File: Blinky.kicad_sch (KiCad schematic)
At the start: 0 parts

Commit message: Created schematic and added vicor and precharge stuff, still need to add board connectors for pacmania
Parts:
- added C1, C2: 1uF, Capacitor_THT:C_Rect_L18.0mm_W8.0mm_P15.00mm_FKS3_FKP3, symbol Device:C_Small
- added C4: 4700uF, Capacitor_THT:C_Radial_D12.5mm_H25.0mm_P5.00mm, symbol Device:C_Small
- added C5: 100uF, Capacitor_THT:C_Radial_D12.5mm_H25.0mm_P5.00mm, symbol Device:C_Small
- added D3: LTST-C171KRKT, LED_SMD:LED_0805_2012Metric, symbol Device:LED
- added D4, D5: BZT52C5V1, Diode_SMD:D_SOD-123, symbol Device:D_Zener
- added J1: DTF13-4P-G003, AERO_Connectors:DTF13-4P-G003, symbol AERO_Connectors:DTF13-4P-G003
- added L1: 1uH, Inductor_SMD:L_1008_2520Metric_Pad1.43x2.20mm_HandSolder, symbol Device:L_Small
- added L2: SLC7649S-151KLC, AERO_Inductors:SLC7649S-151KLC, symbol AERO_Inductors:SLC7649S-151KLC
- added Q1, Q2: IPD90P03P404ATMA2, AERO_Transistors:IPD90P03P404ATMA2, symbol AERO_Transistors:IPD90P03P404ATMA2
- added R1, R2: MP925-5.00K-1%, AERO_Resistors:MP925-5.00K-1%_TabUp, symbol AERO_Resistors:MP925-5.00K-1%
- added R11, R3: 1, Resistor_SMD:R_2512_6332Metric_Pad1.40x3.35mm_HandSolder, symbol Device:R_US
- added R12: 500, Resistor_SMD:R_0805_2012Metric_Pad1.20x1.40mm_HandSolder, symbol Device:R_US
- added R13, R14: 22k, Resistor_SMD:R_0603_1608Metric_Pad0.98x0.95mm_HandSolder, symbol Device:R_US
- added U1: DCM4623TD2J13D0T70, AERO_Regulators:DCM4623TD2J13D0T70, symbol AERO_Regulators:DCM4623TD2J13D0T70
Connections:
- new net: D3.1 (K), R12.1
- new net: D4.2 (A), Q1.2 (G), R13.1
- new net: C1.1, C2.1, L1.2, R3.1, U1.1 (+IN)
- new net: D5.2 (A), Q2.2 (G), R14.1
- new net EN_HV: U1.3 (EN)
- new net FAULT_HV: U1.4 (FT)
- new net INVERTER+: L1.1, R1.2, R3.2
- new net INVERTER-: C1.2, C2.2, R2.1, U1.5 (-IN)
- new net LV_GND: C4.2, C5.2, R12.2, R13.2, R14.2, U1.9 (-OUT)
- new net PRECHARGE_RELAY: R1.1, R2.2
- new net TRIM_HV: U1.2 (TR)
- new net VICOR_FILTERED: C5.1, D3.2 (A), L2.2, Q1.1 (D), Q2.1 (D), R11.1
- new net VICOR_OUT: D4.1 (K), D5.1 (K), J1.1 (Pin_1), J1.2 (Pin_2), J1.3 (Pin_3), J1.4 (Pin_4), Q1.3 (S), Q2.3 (S)
- new net VICOR_RAW: C4.1, L2.1, R11.2, U1.8 (+OUT)
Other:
- note added: "0.25W"
- note added: "500V-rated caps"
- note added: "HIGH VOLTAGE"
- note added: "HV->12V DC-DC"
- note added: "Input Filtering"
- note added: "Output Filtering"
- note added: "max input current ~= 0.81 A"

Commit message: Added connectors
This light will be the death of me
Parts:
- added J2, J3, J4: Conn_01x01, symbol Connector_Generic:Conn_01x01
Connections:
- net INVERTER+: now also J2.1 (Pin_1)
- net INVERTER-: now also J3.1 (Pin_1)
- net PRECHARGE_RELAY: now also J4.1 (Pin_1)

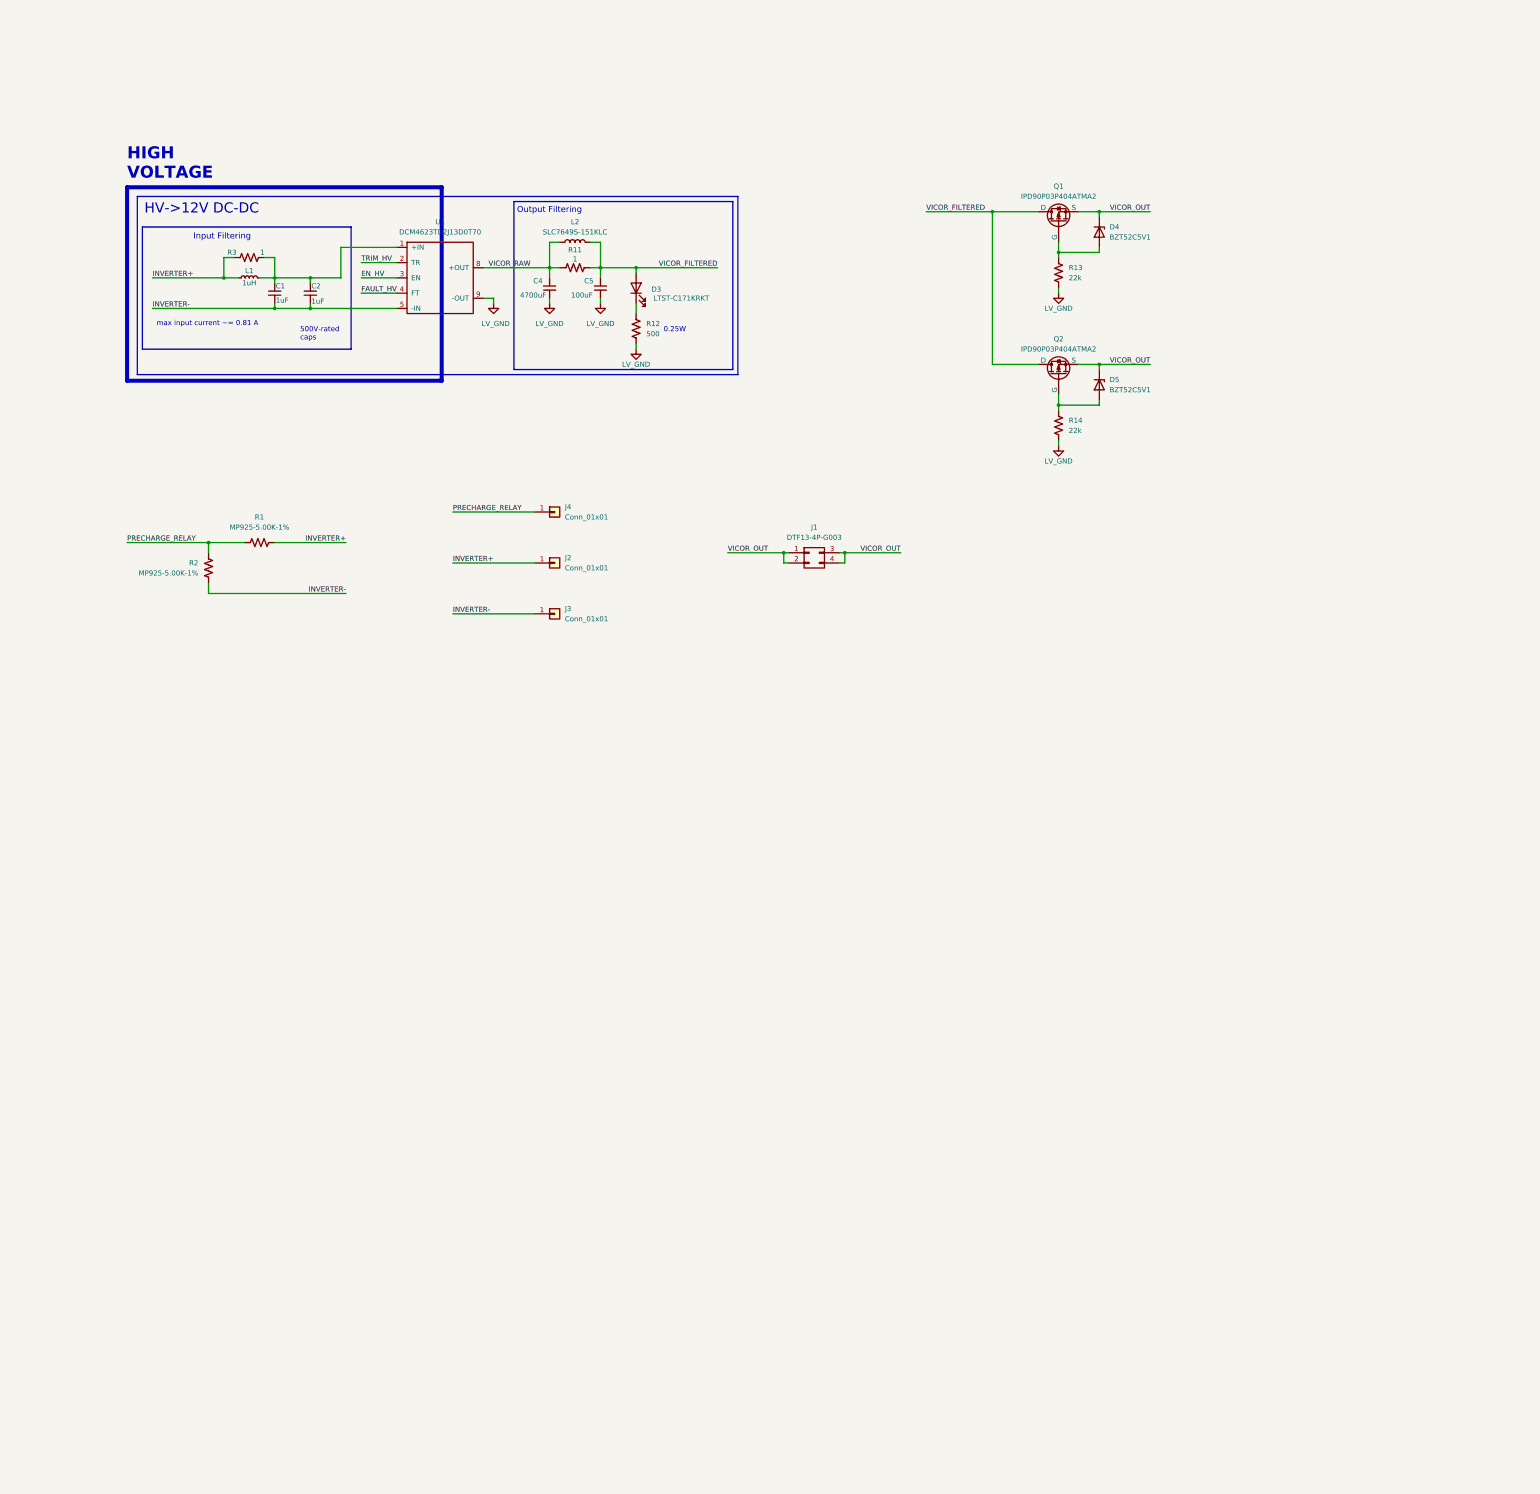
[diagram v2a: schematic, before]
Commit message: Added more final circuit for HV indicator LED, need to update values and footprints
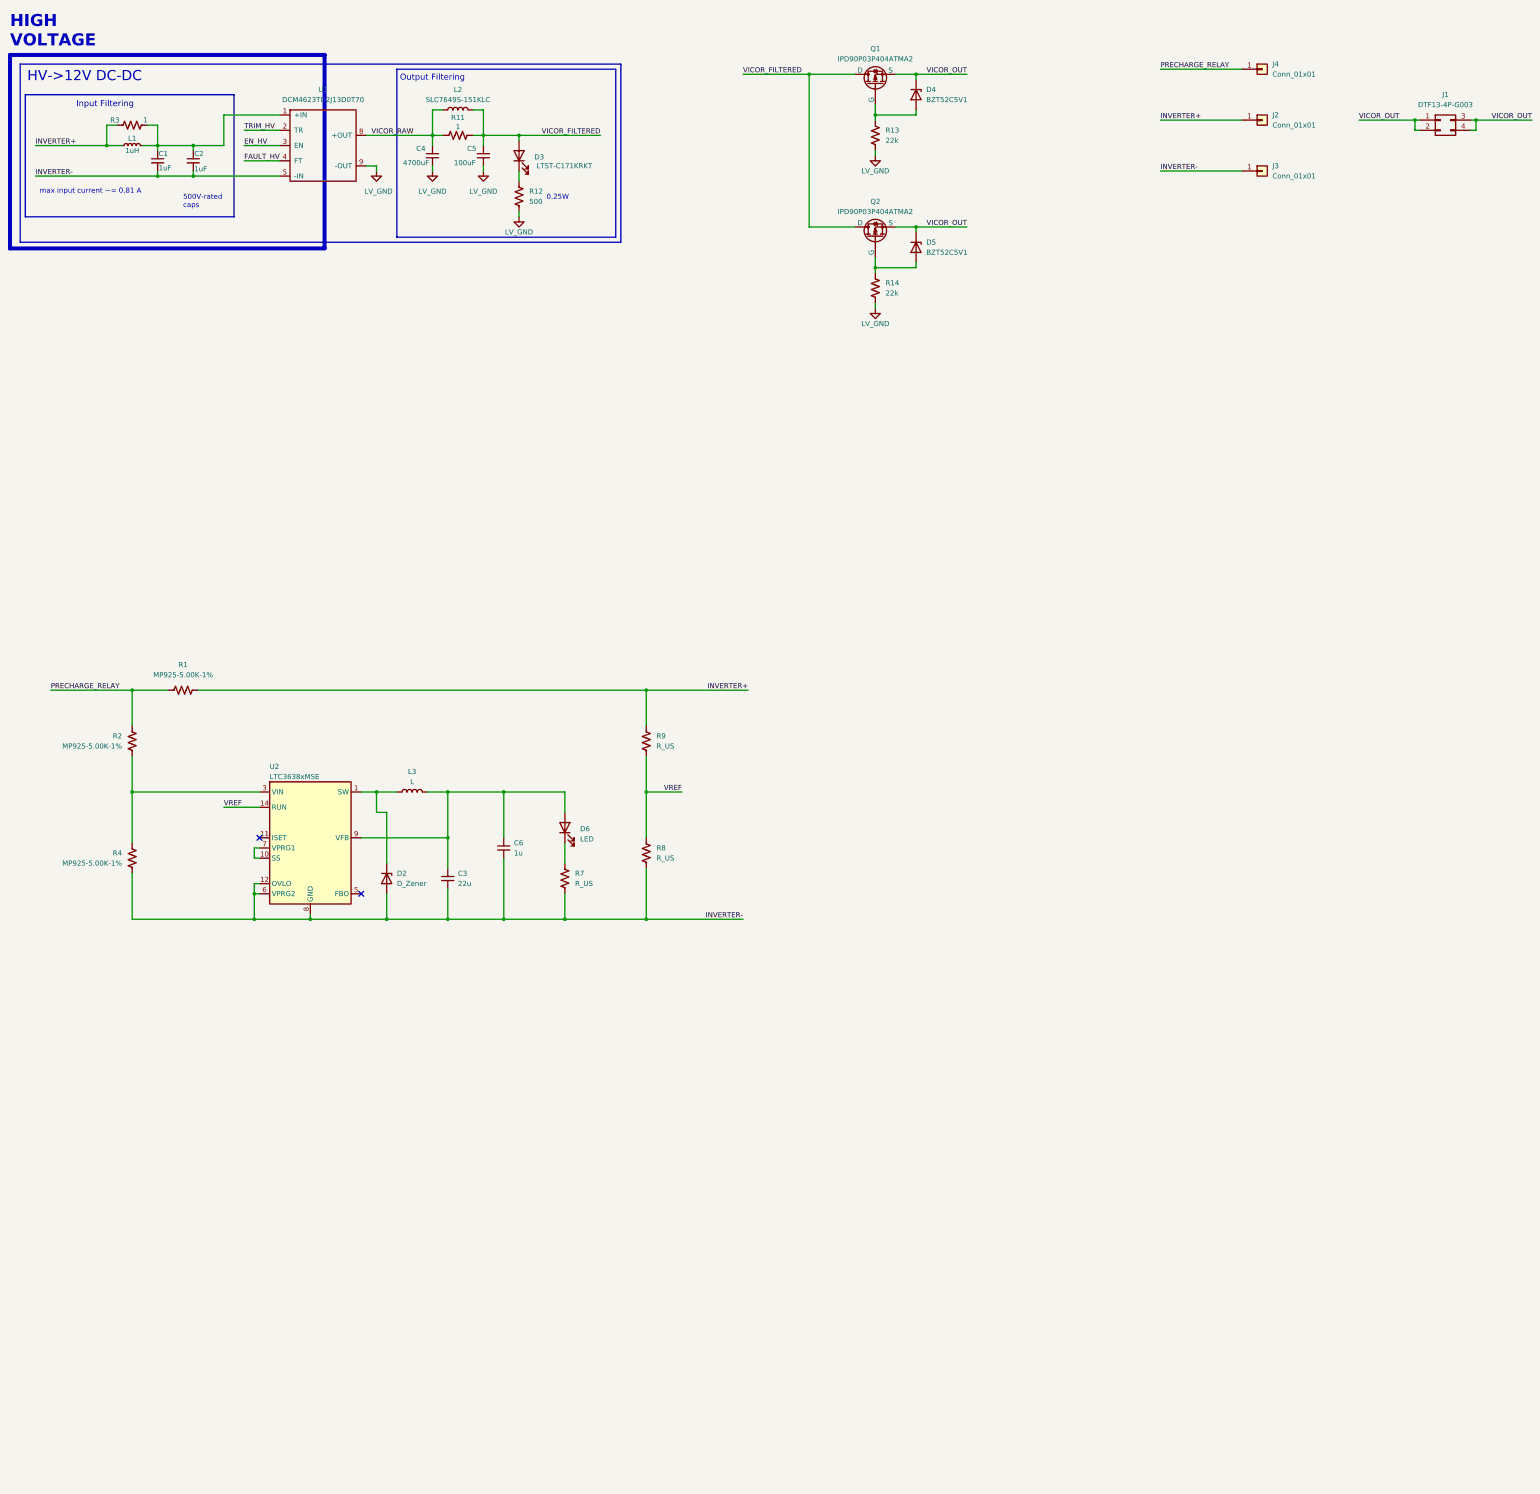
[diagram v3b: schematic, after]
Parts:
- added C3: 22u, Capacitor_SMD:C_0603_1608Metric_Pad1.08x0.95mm_HandSolder, symbol Device:C_Small
- added C6: 1u, Capacitor_SMD:C_0603_1608Metric_Pad1.08x0.95mm_HandSolder, symbol Device:C_Small
- added D2: D_Zener, symbol Device:D_Zener
- added D6: LED, symbol Device:LED
- added L3: L, symbol Device:L
- added R4: MP925-5.00K-1%, AERO_Resistors:MP925-5.00K-1%_TabUp, symbol AERO_Resistors:MP925-5.00K-1%
- added R7, R8, R9: R_US, Resistor_SMD:R_0805_2012Metric_Pad1.20x1.40mm_HandSolder, symbol Device:R_US
- added U2: LTC3638xMSE, Package_SO:Analog_MSOP-12-16-1EP_3x4.039mm_P0.5mm_EP1.651x2.845mm, symbol AERO_Regulators:LTC3638xMSE
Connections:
- net INVERTER+: now also R9.1
- net INVERTER-: now also C3.2, C6.2, D2.2 (A), R4.1, R7.2, R8.2, U2.12 (OVLO), U2.16 (GND), U2.17 (GND), U2.6 (VPRG2), U2.8 (GND); no longer R2.1
- new net: R2.1, R4.2, U2.3 (VIN)
- new net: D2.1 (K), L3.1, U2.1 (SW)
- new net: U2.10 (SS), U2.7 (VPRG1)
- new net: C3.1, C6.1, D6.2 (A), L3.2, U2.9 (VFB)
- new net: D6.1 (K), R7.1
- new net VREF: R8.1, R9.2, U2.14 (RUN)
- no-connect marks 0 -> 2
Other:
- moved on the sheet: C1, C2, C4, C5, D3, D4, D5, J1, J2, J3, J4, L1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

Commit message: Adjusted buck converter circuit
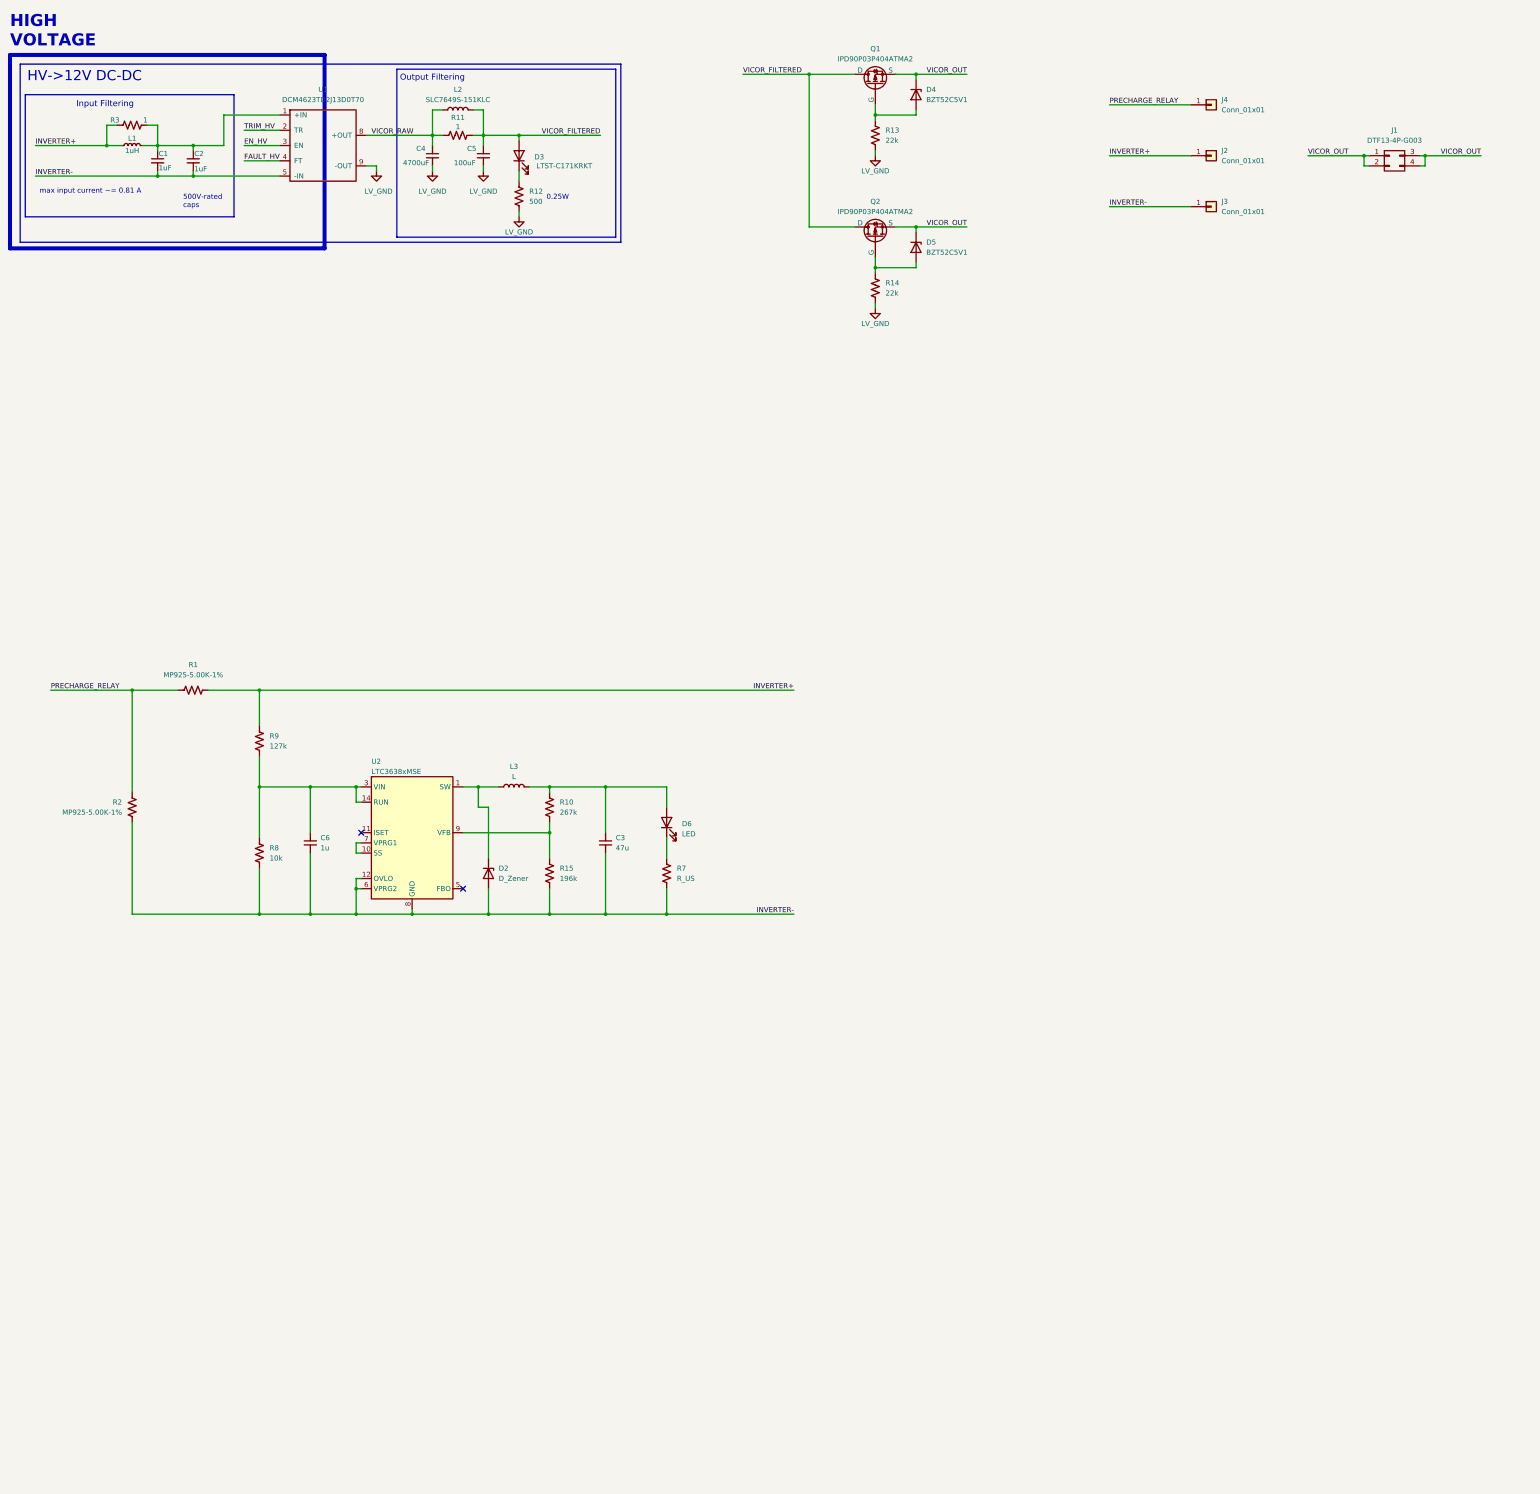
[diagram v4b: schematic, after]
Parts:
- removed R4: MP925-5.00K-1%, AERO_Resistors:MP925-5.00K-1%_TabUp, symbol AERO_Resistors:MP925-5.00K-1%
- added R10: 267k, Resistor_SMD:R_1206_3216Metric_Pad1.30x1.75mm_HandSolder, symbol Device:R_US
- added R15: 196k, Resistor_SMD:R_1206_3216Metric_Pad1.30x1.75mm_HandSolder, symbol Device:R_US
- C3: value 22u -> 47u
- R7: footprint Resistor_SMD:R_0805_2012Metric_Pad1.20x1.40mm_HandSolder -> Resistor_SMD:R_1206_3216Metric_Pad1.30x1.75mm_HandSolder
- R8: value R_US -> 10k; footprint Resistor_SMD:R_0805_2012Metric_Pad1.20x1.40mm_HandSolder -> Resistor_SMD:R_1206_3216Metric_Pad1.30x1.75mm_HandSolder
- R9: value R_US -> 127k; footprint Resistor_SMD:R_0805_2012Metric_Pad1.20x1.40mm_HandSolder -> Resistor_SMD:R_1206_3216Metric_Pad1.30x1.75mm_HandSolder
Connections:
- net VREF is gone; now on an unnamed net: R8.1, R9.2, U2.14 (RUN)
- net INVERTER-: now also R2.1, R15.2
- net at U2.3 (VIN): now also C6.1; no longer R2.1
- net at C3.1, D6.2 (A), L3.2: now also R10.1; no longer C6.1, U2.9 (VFB)
- new net: R10.2, R15.1, U2.9 (VFB)
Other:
- moved on the sheet: D2, D6, J1, J2, J3, J4, L3, R1, R2, R7, R8, R9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
